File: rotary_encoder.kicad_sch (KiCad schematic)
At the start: 2 parts, among them IC10 TLE493DW2B6A0HTSA1

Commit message: added missing MFN numbers
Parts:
- C25: sourced (none) -> y
- IC10: MFN (none) -> 726-TLE493DW2B6A0HTS; sourced (none) -> y
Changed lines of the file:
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@@
+      (effects (font (size 1.27 1.27)) hide)
+    )
+    (property "sourced" "y" (at 144.78 86.36 0)
       (effects (font (size 1.27 1.27)) hide)
     )
@@
       (effects (font (size 1.27 1.27)) (justify left top) hide)
     )
+    (property "MFN" "726-TLE493DW2B6A0HTS " (at 120.65 100.33 0)
+      (effects (font (size 1.27 1.27)) hide)
+    )
+    (property "sourced" "y" (at 120.65 100.33 0)
+      (effects (font (size 1.27 1.27)) hide)
+    )
     (pin "1")

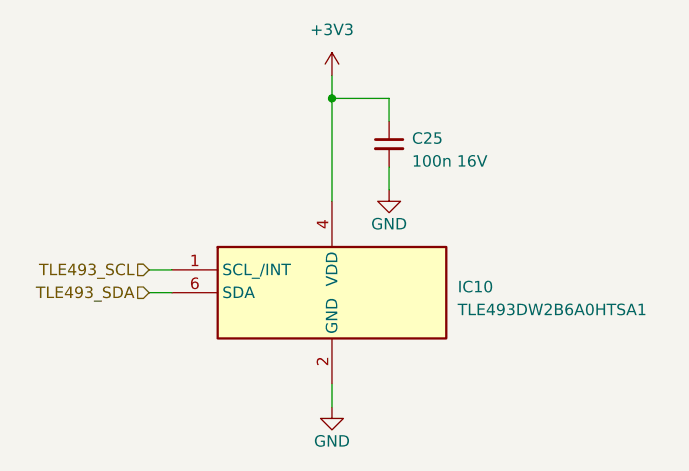
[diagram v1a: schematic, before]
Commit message: Update to KiCad 8 + Add/Fix voltage selector for nRF
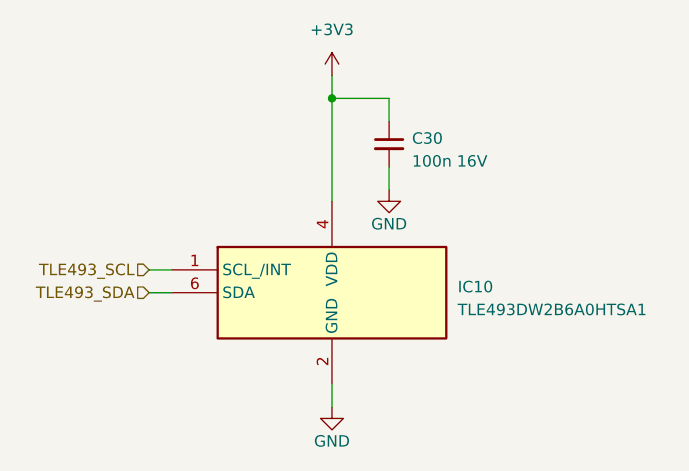
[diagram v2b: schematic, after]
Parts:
- renumbered C25 to C30
